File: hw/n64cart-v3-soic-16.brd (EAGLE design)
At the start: 99.1 x 50.8 mm, 37 parts, among them IC1 RP2040-QFN56, J1 N64_EDGE, Q1 BSS84, U4 MX66L1G45GMI-08G

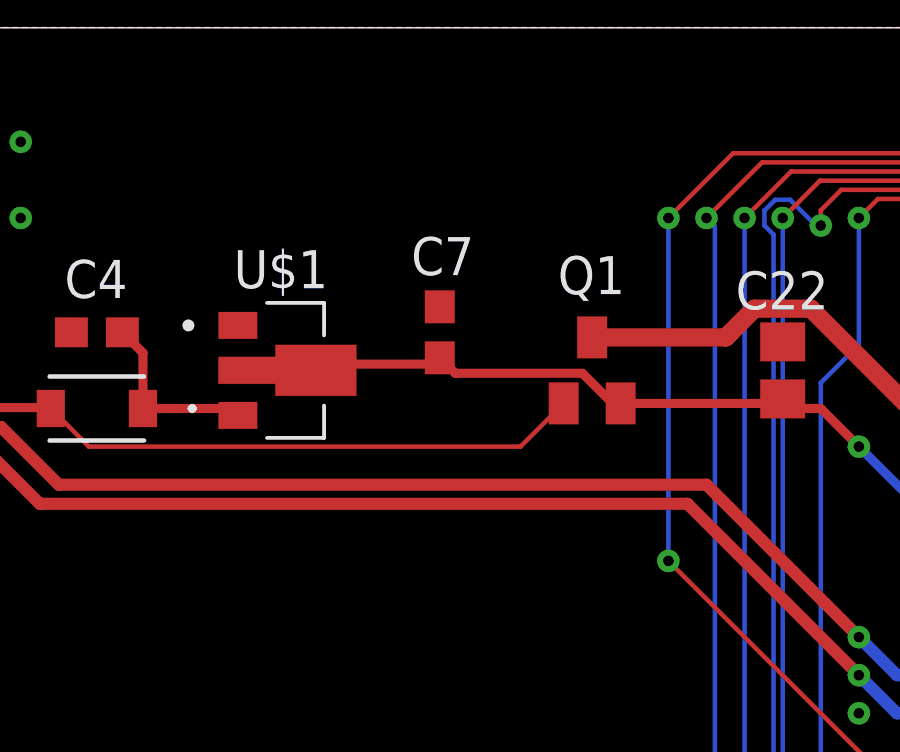
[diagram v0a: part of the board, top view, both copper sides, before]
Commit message: missed pull down resistor for V3
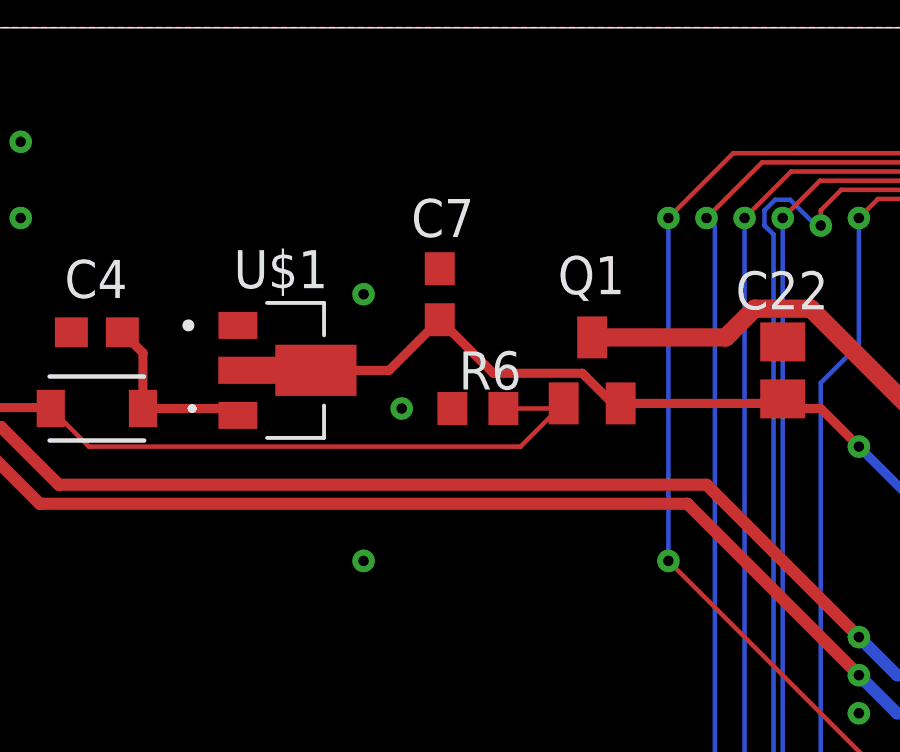
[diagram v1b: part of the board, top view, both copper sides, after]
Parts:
- added R6: 10K, rcl:R0603
- moved C7 1.27 mm to (21.6, 53.3)
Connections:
- net +VBUS: now also R6.2
- net GND: now also R6.1
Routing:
- net +VBUS: track 22.9 -> 24.7 mm
- net +3V3: track 155.5 -> 156.7 mm
- net GND: vias 166 -> 169
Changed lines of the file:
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@@
 <attribute name="VALUE" x="10.795" y="53.975" size="1.27" layer="27" rot="R180"/>
 </element>
-<element name="C7" library="rcl" library_urn="urn:adsk.eagle:library:334" package="C0603" package3d_urn="urn:adsk.eagle:package:23616/2" value="100n" x="21.59" y="52.07" smashed="yes" rot="R90">
-<attribute name="NAME" x="22.733" y="55.245" size="1.27" layer="25" rot="R180"/>
-<attribute name="POPULARITY" value="73" x="21.59" y="52.07" size="1.778" layer="27" rot="R90" display="off"/>
-<attribute name="SPICEPREFIX" value="C" x="21.59" y="52.07" size="1.778" layer="27" rot="R90" display="off"/>
-<attribute name="VALUE" x="23.495" y="51.435" size="1.27" layer="27" rot="R90"/>
+<element name="C7" library="rcl" library_urn="urn:adsk.eagle:library:334" package="C0603" package3d_urn="urn:adsk.eagle:package:23616/2" value="100n" x="21.59" y="53.34" smashed="yes" rot="R90">
+<attribute name="NAME" x="22.733" y="56.515" size="1.27" layer="25" rot="R180"/>
+<attribute name="POPULARITY" value="73" x="21.59" y="53.34" size="1.778" layer="27" rot="R90" display="off"/>
+<attribute name="SPICEPREFIX" value="C" x="21.59" y="53.34" size="1.778" layer="27" rot="R90" display="off"/>
+<attribute name="VALUE" x="23.495" y="52.705" size="1.27" layer="27" rot="R90"/>
 </element>
 <element name="U4" library="MX66L1G45GMI-08G" package="SOP_16L_300_MAC-L" value="MX66L1G45GMI-08G" x="45.72" y="26.67" smashed="yes" rot="R45">
@@
 <attribute name="MFR_NAME" value="Vishay" x="10.16" y="49.53" size="1.778" layer="27" rot="R180" display="off"/>
 <attribute name="NAME" x="12.1666" y="47.625" size="1.27" layer="27" ratio="6" rot="SR180"/>
+</element>
+<element name="R6" library="rcl" library_urn="urn:adsk.eagle:library:334" package="R0603" package3d_urn="urn:adsk.eagle:package:23555/3" value="10K" x="22.86" y="49.53" smashed="yes">
+<attribute name="NAME" x="22.225" y="50.165" size="1.27" layer="25"/>
+<attribute name="POPULARITY" value="70" x="22.86" y="49.53" size="1.778" layer="27" display="off"/>
+<attribute name="SPICEPREFIX" value="R" x="22.86" y="49.53" size="1.778" layer="27" display="off"/>
+<attribute name="VALUE" x="22.225" y="47.625" size="1.27" layer="27"/>
 </element>
 </elements>
@@
 <via x="81.28" y="53.34" extent="1-16" drill="0.35"/>
 <contactref element="D2" pad="C"/>
+<contactref element="R6" pad="1"/>
+<via x="19.05" y="53.34" extent="1-16" drill="0.35"/>
+<via x="20.32" y="49.53" extent="1-16" drill="0.35"/>
+<via x="19.05" y="44.45" extent="1-16" drill="0.35"/>
 </signal>
 <signal name="+3V3">
@@
 <wire x1="16.51" y1="50.8" x2="16.93" y2="51.22" width="0.6096" layer="1"/>
 <wire x1="27.62" y1="49.7" x2="27.35105" y2="49.7" width="0.3048" layer="1"/>
-<wire x1="27.35105" y1="49.7" x2="26.34625" y2="50.7048" width="0.3048" layer="1"/>
-<wire x1="22.1052" y1="50.7048" x2="21.8" y2="51.01" width="0.3048" layer="1"/>
-<wire x1="21.8" y1="51.01" x2="21.59" y2="51.22" width="0.3048" layer="1"/>
-<wire x1="26.34625" y1="50.7048" x2="22.1052" y2="50.7048" width="0.3048" layer="1"/>
+<wire x1="26.460525" y1="50.590525" x2="27.35105" y2="49.7" width="0.3048" layer="1"/>
 <wire x1="16.51" y1="50.8" x2="16.72" y2="51.01" width="0.3048" layer="1"/>
-<wire x1="16.72" y1="51.01" x2="21.8" y2="51.01" width="0.3048" layer="1"/>
 <wire x1="27.62" y1="49.7" x2="32.85" y2="49.7" width="0.3048" layer="1"/>
 <wire x1="32.85" y1="49.7" x2="32.86" y2="49.69" width="0.3048" layer="1"/>
+<wire x1="16.51" y1="50.8" x2="19.9" y2="50.8" width="0.3048" layer="1"/>
+<wire x1="19.9" y1="50.8" x2="21.59" y2="52.49" width="0.3048" layer="1"/>
+<wire x1="26.34625" y1="50.7048" x2="26.460525" y2="50.590525" width="0.3048" layer="1"/>
+<wire x1="21.59" y1="52.49" x2="23.3752" y2="50.7048" width="0.3048" layer="1"/>
+<wire x1="23.3752" y1="50.7048" x2="26.34625" y2="50.7048" width="0.3048" layer="1"/>
 </signal>
 <signal name="AD15_C">
@@
 <wire x1="8.5933" y1="49.56" x2="8.6233" y2="49.53" width="0.3048" layer="1"/>
 <wire x1="8.6233" y1="49.53" x2="9.8933" y2="48.26" width="0.1524" layer="1"/>
-<wire x1="24.28" y1="48.26" x2="25.72" y2="49.7" width="0.1524" layer="1"/>
+<wire x1="24.28" y1="48.26" x2="25.475" y2="49.455" width="0.1524" layer="1"/>
+<wire x1="25.475" y1="49.455" x2="25.72" y2="49.7" width="0.1524" layer="1"/>
 <wire x1="9.8933" y1="48.26" x2="24.28" y2="48.26" width="0.1524" layer="1"/>
+<contactref element="R6" pad="2"/>
+<wire x1="23.71" y1="49.53" x2="25.4" y2="49.53" width="0.1524" layer="1"/>
+<wire x1="25.4" y1="49.53" x2="25.475" y2="49.455" width="0.1524" layer="1"/>
 </signal>
 <signal name="SWCLK">
